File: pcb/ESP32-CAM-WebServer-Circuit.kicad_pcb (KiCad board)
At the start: 2 copper layers, 30.5 x 48.3 mm, 12 parts, among them IC1 ESP32-CAM, J1 Conn_01x02, Q1 2N7002, Q2 IRLML0030, SW1 SW_SPDT, U1 TP4056-Module, U2 XC6503D331MR-G

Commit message: Update PCB with changes made to schematics
These changes refer to those made by the following commits:
Commit ac1b94ba7ff7763ca98be71d2aac60c6ba4cc6ba.
Commit 95e476ec9aa6ccc7e2e980449346e72e7ed39c10.
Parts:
- SW1: value SW_SPDT -> EG1270
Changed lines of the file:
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@@
     (descr "SOT, 5 Pin (https://www.jedec.org/sites/default/files/docs/Mo-178c.PDF variant AA), generated with kicad-footprint-generator ipc_gullwing_generator.py")
     (tags "SOT TO_SOT_SMD")
+    (property "Farnell Nr" "3535464")
     (property "Sheetfile" "ESP32-CAM-WebServer-Circuit.kicad_sch")
     (property "Sheetname" "")
@@
     (descr "SOT, 3 Pin (https://www.jedec.org/system/files/docs/to-236h.pdf variant AB), generated with kicad-footprint-generator ipc_gullwing_generator.py")
     (tags "SOT TO_SOT_SMD")
+    (property "Farnell Nr" "2706627")
     (property "Sheetfile" "ESP32-CAM-WebServer-Circuit.kicad_sch")
     (property "Sheetname" "")
@@
       (effects (font (size 1.27 1.27) (thickness 0.254)) (justify mirror))
     )
-    (fp_text value "SW_SPDT" (at -1.85 2.5 90) (layer "B.SilkS") hide
+    (fp_text value "EG1270" (at -1.85 2.5 90) (layer "B.SilkS") hide
       (effects (font (size 1.27 1.27) (thickness 0.254)) (justify mirror))
     )

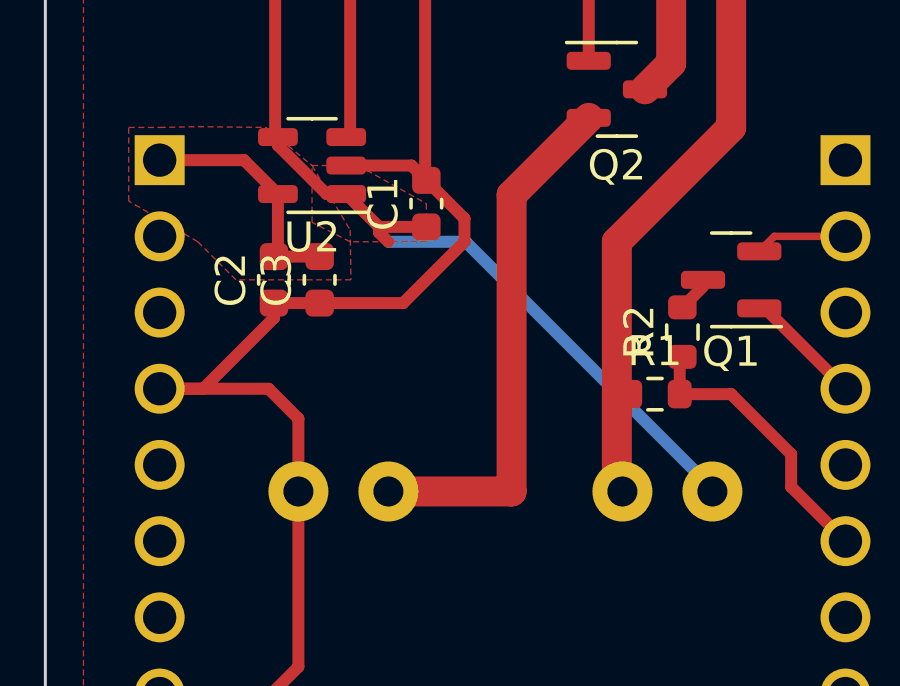
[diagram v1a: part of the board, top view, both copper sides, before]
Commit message: Revert "Move LiPo- Trace"
This reverts commit be3a369112a36adc4f45e463117a6747faac4736.
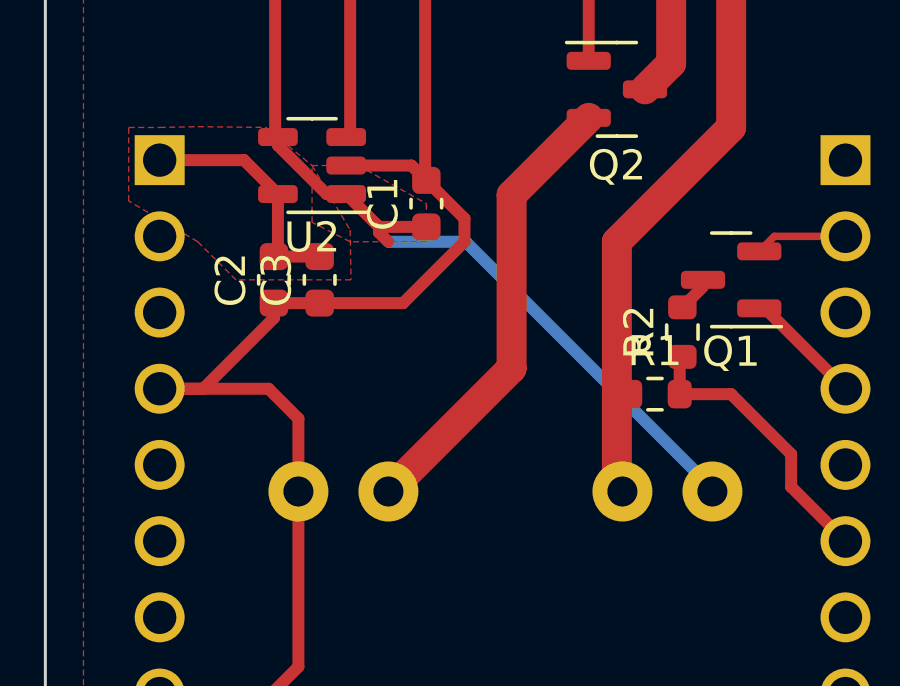
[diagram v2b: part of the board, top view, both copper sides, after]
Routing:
- net LiPo-: track 17.6 -> 15.2 mm
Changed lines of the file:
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@@
   (segment (start 169.45 50.8) (end 169.45 55.0075) (width 1) (layer "F.Cu") (net 17))
   (segment (start 169.45 55.0075) (end 168.5775 55.88) (width 1) (layer "F.Cu") (net 17))
-  (segment (start 164.13067 69.285) (end 160.025 69.285) (width 1) (layer "F.Cu") (net 18))
+  (segment (start 164.13067 59.40183) (end 164.13067 65.17933) (width 1) (layer "F.Cu") (net 18))
   (segment (start 166.7025 56.83) (end 164.13067 59.40183) (width 1) (layer "F.Cu") (net 18))
-  (segment (start 164.13067 59.40183) (end 164.13067 69.285) (width 1) (layer "F.Cu") (net 18))
+  (segment (start 164.13067 65.17933) (end 160.025 69.285) (width 1) (layer "F.Cu") (net 18))
   (segment (start 158.75 51.38) (end 158.75 57.3375) (width 0.4) (layer "F.Cu") (net 22))
   (segment (start 158.75 57.3375) (end 158.6175 57.47) (width 0.4) (layer "F.Cu") (net 22))

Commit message: Revert "Revert "Change capacitor value from 1u to 1000n""
This reverts commit bc24fff1710632b99b5469beaa07fc302cc7a78a.
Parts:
- C3: value 1u -> 1000n
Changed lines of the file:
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@@
     )
   )
+  (property "DATE" "2023-06-01")
+  (property "REV" "Git:4fd512b")
   (net 0 "")
   (net 1 "Net-(C1-Pad1)")
@@
       (effects (font (size 1 1) (thickness 0.15)))
     )
-    (fp_text value "1u" (at 0 1.43 90) (layer "F.Fab")
-      (effects (font (size 1 1) (thickness 0.15)))
-    )
+    (fp_text value "1000n" (at 0 1.43 90) (layer "F.Fab")
+      (effects (font (size 1 1) (thickness 0.15)))
+    )

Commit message: Undo capacitor value change on board
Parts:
- C3: value 1000n -> 1u
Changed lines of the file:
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@@
       (effects (font (size 1 1) (thickness 0.15)))
     )
-    (fp_text value "1000n" (at 0 1.43 90) (layer "F.Fab")
+    (fp_text value "1u" (at 0 1.43 90) (layer "F.Fab")
       (effects (font (size 1 1) (thickness 0.15)))
     )
